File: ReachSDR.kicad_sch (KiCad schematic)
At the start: 0 parts

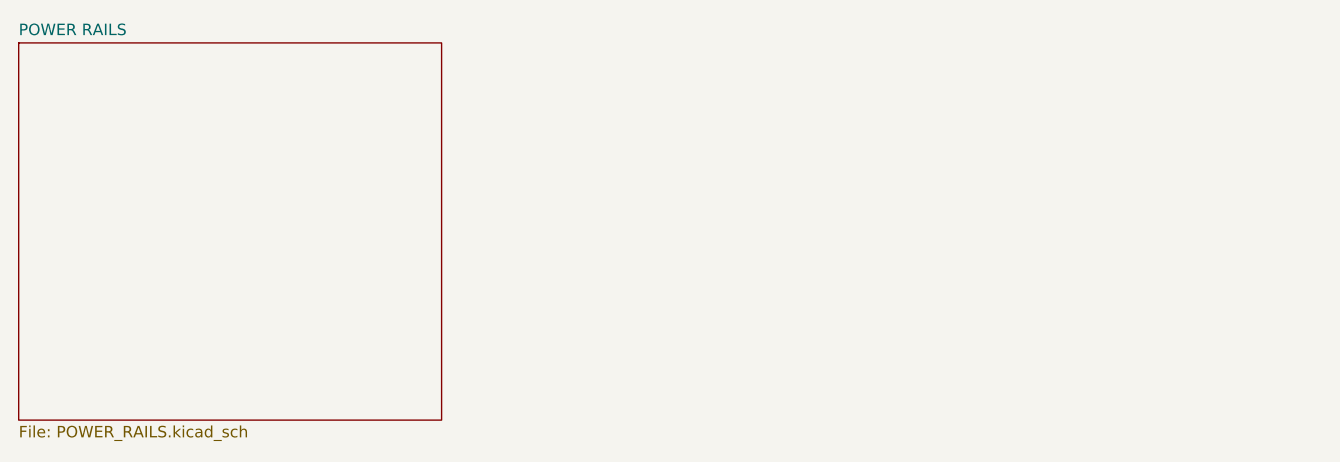
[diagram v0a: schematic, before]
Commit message: Added ADC.kicad_sch and CLOCKS.kicad_sch.
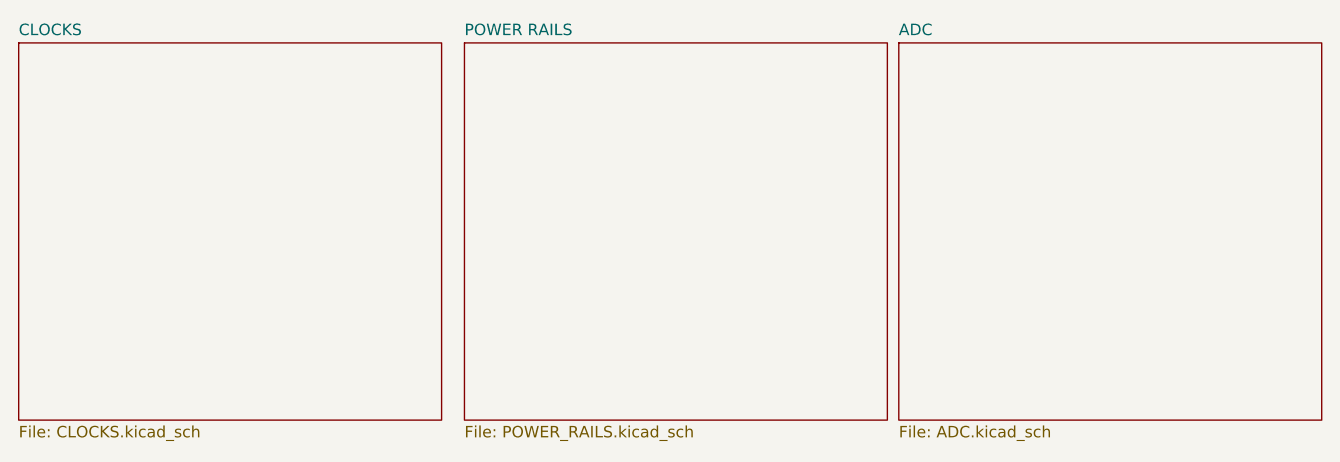
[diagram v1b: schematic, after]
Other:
- added sheet ADC (ADC.kicad_sch)
- added sheet CLOCKS (CLOCKS.kicad_sch)
- company: (none) -> //COLDJOINT
- title: (none) -> ReachSDR
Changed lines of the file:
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@@
 	(generator_version "9.0")
 	(paper "A4")
+	(title_block
+		(title "ReachSDR")
+		(rev "REV A")
+		(company "//COLDJOINT")
+		(comment 1 "HTTPS://COLDJOINT.XYZ")
+	)
+	(sheet
+		(at 62.23 15.24)
+		(size 46.99 41.91)
+		(exclude_from_sim no)
+		(in_bom yes)
+		(on_board yes)
+		(dnp no)
+		(fields_autoplaced yes)
+		(stroke
+			(width 0.1524)
+			(type solid)
+		)
+		(fill
+			(color 0 0 0 0.0000)
+		)
+		(property "Sheetname" "POWER RAILS"
+			(at 62.23 14.5284 0)
+			(effects
+				(font
+					(size 1.27 1.27)
+				)
+				(justify left bottom)
+			)
+		)
+		(property "Sheetfile" "POWER_RAILS.kicad_sch"
+			(at 62.23 57.7346 0)
+			(effects
+				(font
+					(size 1.27 1.27)
+				)
+				(justify left top)
+			)
+		)
+		(instances
+			(project "ReachSDR"
+				(path "/db2c5d43-db60-4f79-87a7-e62926853608"
+					(page "2")
+				)
+			)
+		)
+	)
+	(sheet
+		(at 110.49 15.24)
+		(size 46.99 41.91)
+		(exclude_from_sim no)
+		(in_bom yes)
+		(on_board yes)
+		(dnp no)
+		(fields_autoplaced yes)
+		(stroke
+			(width 0.1524)
+			(type solid)
+		)
+		(fill
+			(color 0 0 0 0.0000)
+		)
+		(property "Sheetname" "ADC"
+			(at 110.49 14.5284 0)
+			(effects
+				(font
+					(size 1.27 1.27)
+				)
+				(justify left bottom)
+			)
+		)
+		(property "Sheetfile" "ADC.kicad_sch"
+			(at 110.49 57.7346 0)
+			(effects
+				(font
+					(size 1.27 1.27)
+				)
+				(justify left top)
+			)
+		)
+		(instances
+			(project "ReachSDR"
+				(path "/db2c5d43-db60-4f79-87a7-e62926853608"
+					(page "4")
+				)
+			)
+		)
+	)
 	(sheet
 		(at 12.7 15.24)
@@
 			(color 0 0 0 0.0000)
 		)
-		(property "Sheetname" "POWER RAILS"
+		(property "Sheetname" "CLOCKS"
 			(at 12.7 14.5284 0)
 			(effects
@@
 			)
 		)
-		(property "Sheetfile" "POWER_RAILS.kicad_sch"
+		(property "Sheetfile" "CLOCKS.kicad_sch"
 			(at 12.7 57.7346 0)
 			(effects
@@
 			(project "ReachSDR"
 				(path "/db2c5d43-db60-4f79-87a7-e62926853608"
-					(page "2")
+					(page "3")
 				)
 			)
